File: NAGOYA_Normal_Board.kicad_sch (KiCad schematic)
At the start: 99 parts, among them CN1 XT30-M, CN13 value, CN14 RefereeSystem, CN15 micro_B, CN2 XT30-M, CN3 XT30-F, CN4 XT30-F, CN5 XT30-F, CN6 XT30-F, J1 debug, J10 CAN3, J13 CAN3, J14 CAN3, J5 CAN3, J6 CAN3, J7 CAN3, J8 CAN3, J9 CAN3, Q2 DDTC114EUA-7-F, Q4 DDTC114EUA-7-F, Q5 DDTC114EUA-7-F, Q6 DDTC114EUA-7-F, U1 Teensy4.1, U2 TCAN1042HVDR, U3 TCAN1042HVDR, U4 TCAN1042HVDR, U5 FT234XD, U6 TLP172AM, U7 BNO055, U8 ADuM121N, U9 LXES11DAA2-137, Y2 32.768 k

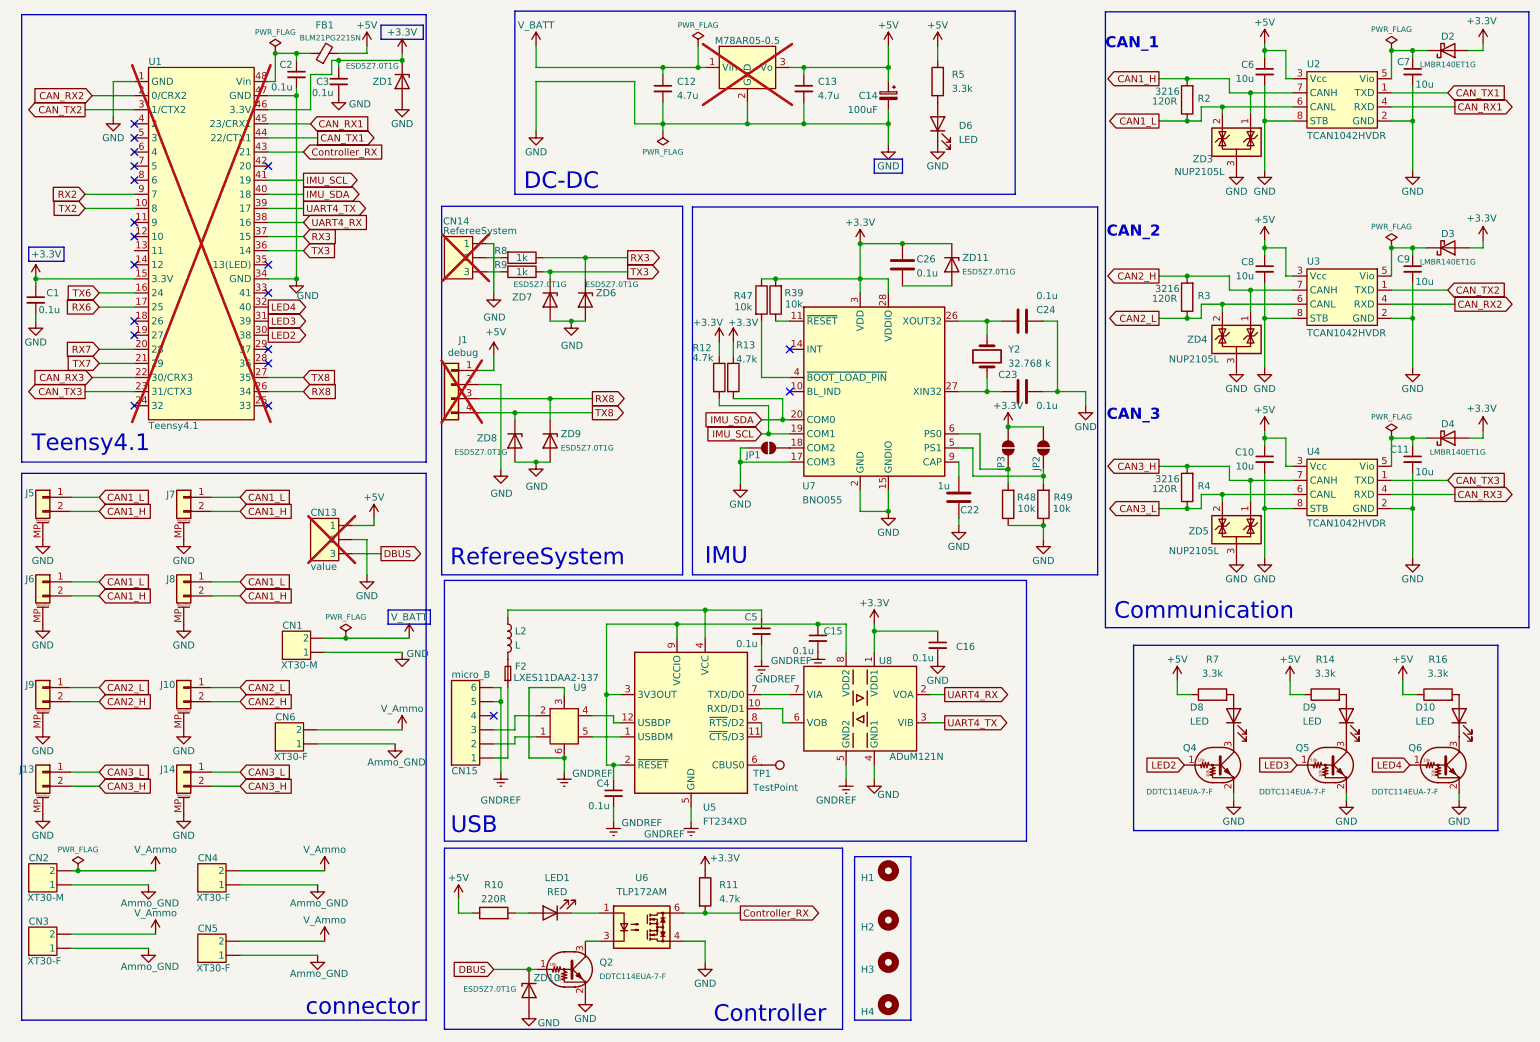
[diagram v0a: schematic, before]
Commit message: USBシリアルを絶縁
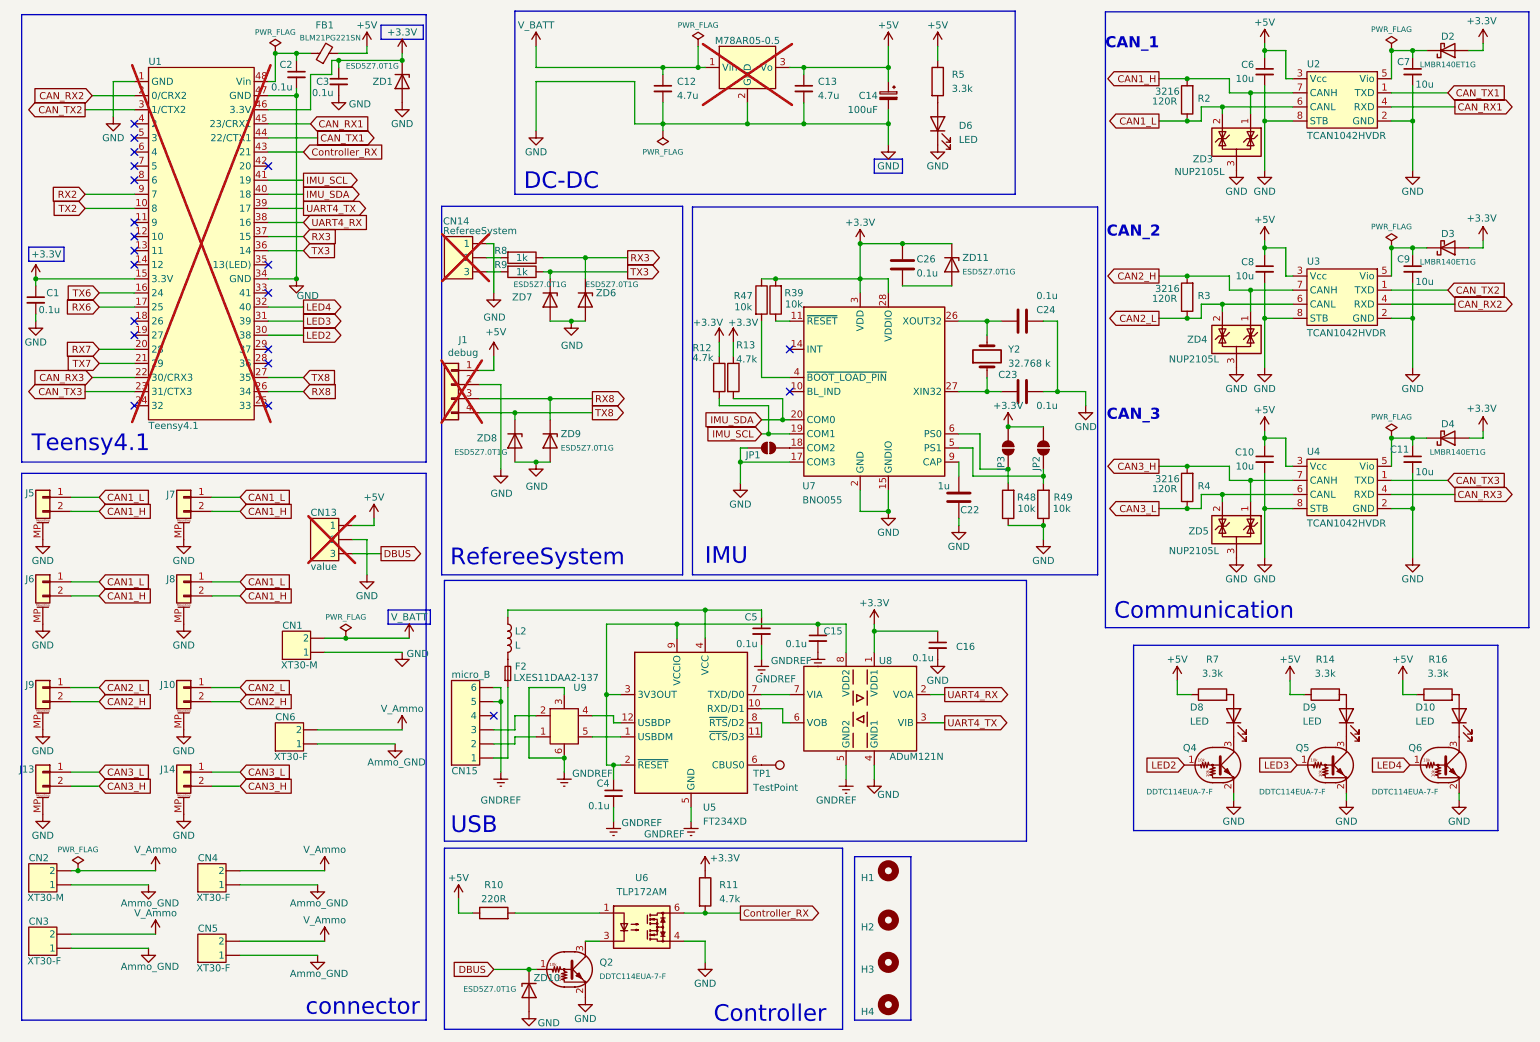
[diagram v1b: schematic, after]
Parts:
- removed LED1: RED, LED_SMD:LED_0603_1608Metric, symbol Device:LED
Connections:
- net at U6.1: now also R10.2
- no-connect marks 20 -> 21
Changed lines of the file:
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@@
 	)
 	(no_connect
+		(at 33.02 55.88)
+	)
+	(no_connect
 		(at 57.15 63.5)
 	)
@@
 	(wire
 		(pts
+			(xy 57.15 68.58) (xy 63.5 68.58)
+		)
+		(stroke
+			(width 0)
+			(type default)
+		)
+	)
+	(wire
+		(pts
 			(xy 236.728 55.372) (xy 236.728 56.642)
 		)
@@
 	(wire
 		(pts
+			(xy 57.15 71.12) (xy 63.5 71.12)
+		)
+		(stroke
+			(width 0)
+			(type default)
+		)
+	)
+	(wire
+		(pts
 			(xy 105.41 25.4) (xy 105.41 34.29)
 		)
@@
 	(wire
 		(pts
+			(xy 57.15 66.04) (xy 63.5 66.04)
+		)
+		(stroke
+			(width 0)
+			(type default)
+		)
+	)
+	(wire
+		(pts
 			(xy 107.95 82.55) (xy 107.95 86.36)
 		)
@@
 	(wire
 		(pts
-			(xy 104.14 175.26) (xy 101.6 175.26)
+			(xy 101.6 175.26) (xy 116.84 175.26)
 		)
 		(stroke
@@
 	(wire
 		(pts
-			(xy 111.76 175.26) (xy 116.84 175.26)
-		)
-		(stroke
-			(width 0)
-			(type default)
-		)
-	)
-	(wire
-		(pts
 			(xy 104.14 134.62) (xy 104.14 147.32)
 		)
@@
 	(global_label "LED4"
 		(shape output)
-		(at 57.15 66.04 0)
+		(at 63.5 66.04 0)
 		(fields_autoplaced yes)
 		(effects
@@
 		)
 		(property "Intersheetrefs" "${INTERSHEET_REFS}"
-			(at 64.7918 66.04 0)
+			(at 71.1418 66.04 0)
 			(effects
 				(font
@@
 	(global_label "LED3"
 		(shape output)
-		(at 57.15 68.58 0)
+		(at 63.5 68.58 0)
 		(fields_autoplaced yes)
 		(effects
@@
 		)
 		(property "Intersheetrefs" "${INTERSHEET_REFS}"
-			(at 64.7918 68.58 0)
+			(at 71.1418 68.58 0)
 			(effects
 				(font
@@
 	(global_label "LED2"
 		(shape output)
-		(at 57.15 71.12 0)
+		(at 63.5 71.12 0)
 		(fields_autoplaced yes)
 		(effects
@@
 		)
 		(property "Intersheetrefs" "${INTERSHEET_REFS}"
-			(at 64.7918 71.12 0)
+			(at 71.1418 71.12 0)
 			(effects
 				(font
@@
 	)
 	(symbol
-		(lib_id "Device:LED")
-		(at 107.95 175.26 180)
-		(unit 1)
-		(exclude_from_sim no)
-		(in_bom yes)
-		(on_board yes)
-		(dnp no)
-		(property "Reference" "LED1"
-			(at 109.22 168.91 0)
-			(effects
-				(font
-					(size 1.27 1.27)
-				)
-			)
-		)
-		(property "Value" "RED"
-			(at 109.22 171.45 0)
-			(effects
-				(font
-					(size 1.27 1.27)
-				)
-			)
-		)
-		(property "Footprint" "LED_SMD:LED_0603_1608Metric"
-			(at 107.95 175.26 0)
-			(effects
-				(font
-					(size 1.27 1.27)
-				)
-				(hide yes)
-			)
-		)
-		(property "Datasheet" "https://wmsc.lcsc.com/wmsc/upload/file/pdf/v2/lcsc/2304140030_ROHM-Semicon-SML-D12U8WT86_C510027.pdf"
-			(at 107.95 175.26 0)
-			(effects
-				(font
-					(size 1.27 1.27)
-				)
-				(hide yes)
-			)
-		)
-		(property "Description" "Light emitting diode"
-			(at 107.95 175.26 0)
-			(effects
-				(font
-					(size 1.27 1.27)
-				)
-				(hide yes)
-			)
-		)
-		(property "メーカ" ""
-			(at 107.95 175.26 90)
-			(effects
-				(font
-					(size 1.27 1.27)
-				)
-				(hide yes)
-			)
-		)
-		(property "購入先" "JLCPCB"
-			(at 107.95 175.26 90)
-			(effects
-				(font
-					(size 1.27 1.27)
-				)
-				(hide yes)
-			)
-		)
-		(property "型番" "SML-D12U8WT86"
-			(at 107.95 175.26 90)
-			(effects
-				(font
-					(size 1.27 1.27)
-				)
-				(hide yes)
-			)
-		)
-		(property "LCSC" "C510027"
-			(at 107.95 175.26 90)
-			(effects
-				(font
-					(size 1.27 1.27)
-				)
-				(hide yes)
-			)
-		)
-		(property "メーカー名" "Rohm"
-			(at 107.95 175.26 0)
-			(effects
-				(font
-					(size 1.27 1.27)
-				)
-				(hide yes)
-			)
-		)
-		(pin "2"
-		)
-		(pin "1"
-		)
-		(instances
-			(project "NAGOYA_Normal_Board"
-				(path "/21c37265-f169-4bc1-832f-6fa8bb337745"
-					(reference "LED1")
-					(unit 1)
-				)
-			)
-		)
-	)
-	(symbol
 		(lib_id "Device:R")
 		(at 97.79 175.26 90)
@@
 		)
 		(property "Value" "0.1u"
-			(at 151.638 128.016 0)
+			(at 150.368 126.746 0)
 			(effects
 				(font

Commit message: 発注用データ
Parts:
- added R50, R51, R52, R53: 10k, Resistor_SMD:R_0603_1608Metric, symbol Device:R
- added SW1: SW_DIP_x04, Button_Switch_SMD:SW_DIP_SPSTx04_Slide_Copal_CHS-04A_W5.08mm_P1.27mm_JPin, symbol Switch:SW_DIP_x04
- C15, C16, C4, C5, CN1, CN2, CN3, CN4, CN5, CN6, F2, JP1, JP2, JP3, L2, TP1, U5, U9: now not fitted
- C22: LCSC (none) -> C15849
- C23, C24, C26: LCSC (none) -> C14663
- CN15: LCSC (none) -> C132563; now not fitted
- J10, J13, J14, J5, J6, J7, J8, J9: LCSC (none) -> C189893
- R39, R47, R48, R49: LCSC (none) -> C25804
- R8, R9: LCSC (none) -> C21190
- U6: LCSC (none) -> C2152276
- U7: LCSC (none) -> C93216
- U8: LCSC (none) -> C660274; now not fitted
- Y2: LCSC (none) -> C32346
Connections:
- net +3.3V: now also R50.2, R51.2, R52.2, R53.2
- net GND: now also SW1.5, SW1.6, SW1.7, SW1.8
- net DIP_SW_4: now reaches U1.11 (9)
- net DIP_SW_4: now also R53.1, SW1.4
- net DIP_SW_3: now reaches U1.12 (10)
- net DIP_SW_3: now also R52.1, SW1.3
- net DIP_SW_2: now reaches U1.13 (11)
- net DIP_SW_2: now also R51.1, SW1.2
- net DIP_SW_1: now reaches U1.14 (12)
- net DIP_SW_1: now also R50.1, SW1.1
- no-connect marks 21 -> 17
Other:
- moved on the sheet: C12, C13, C14, D6, M78AR05-0.5, R5

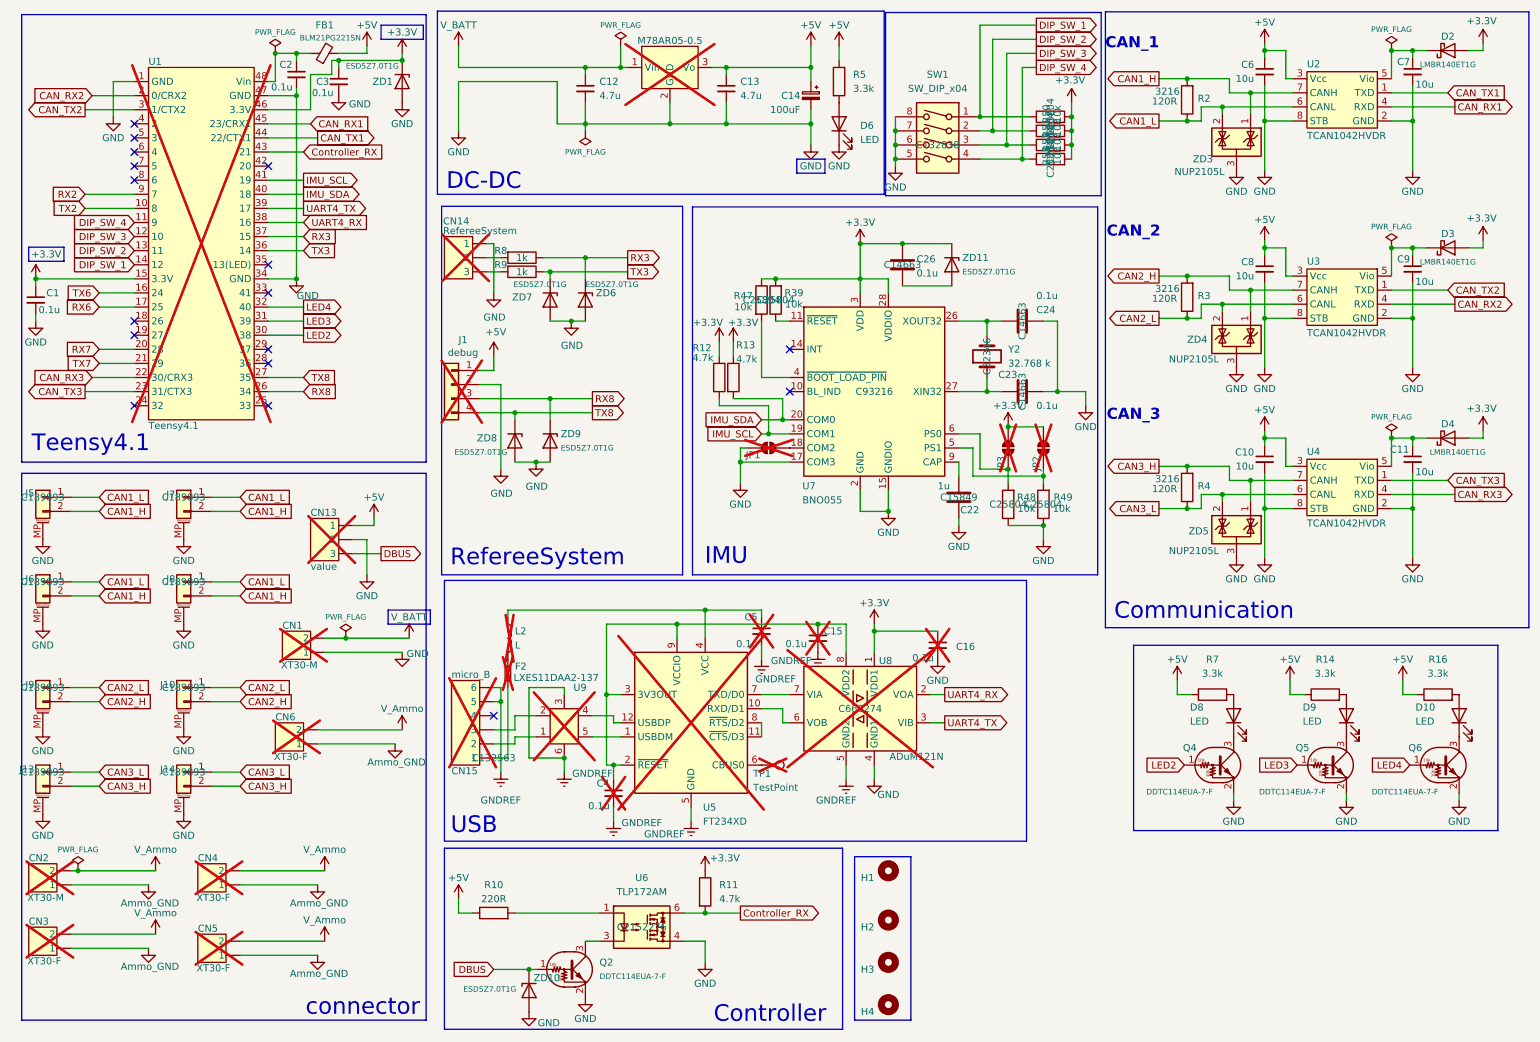
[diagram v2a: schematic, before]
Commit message: 発注用parameterを変更
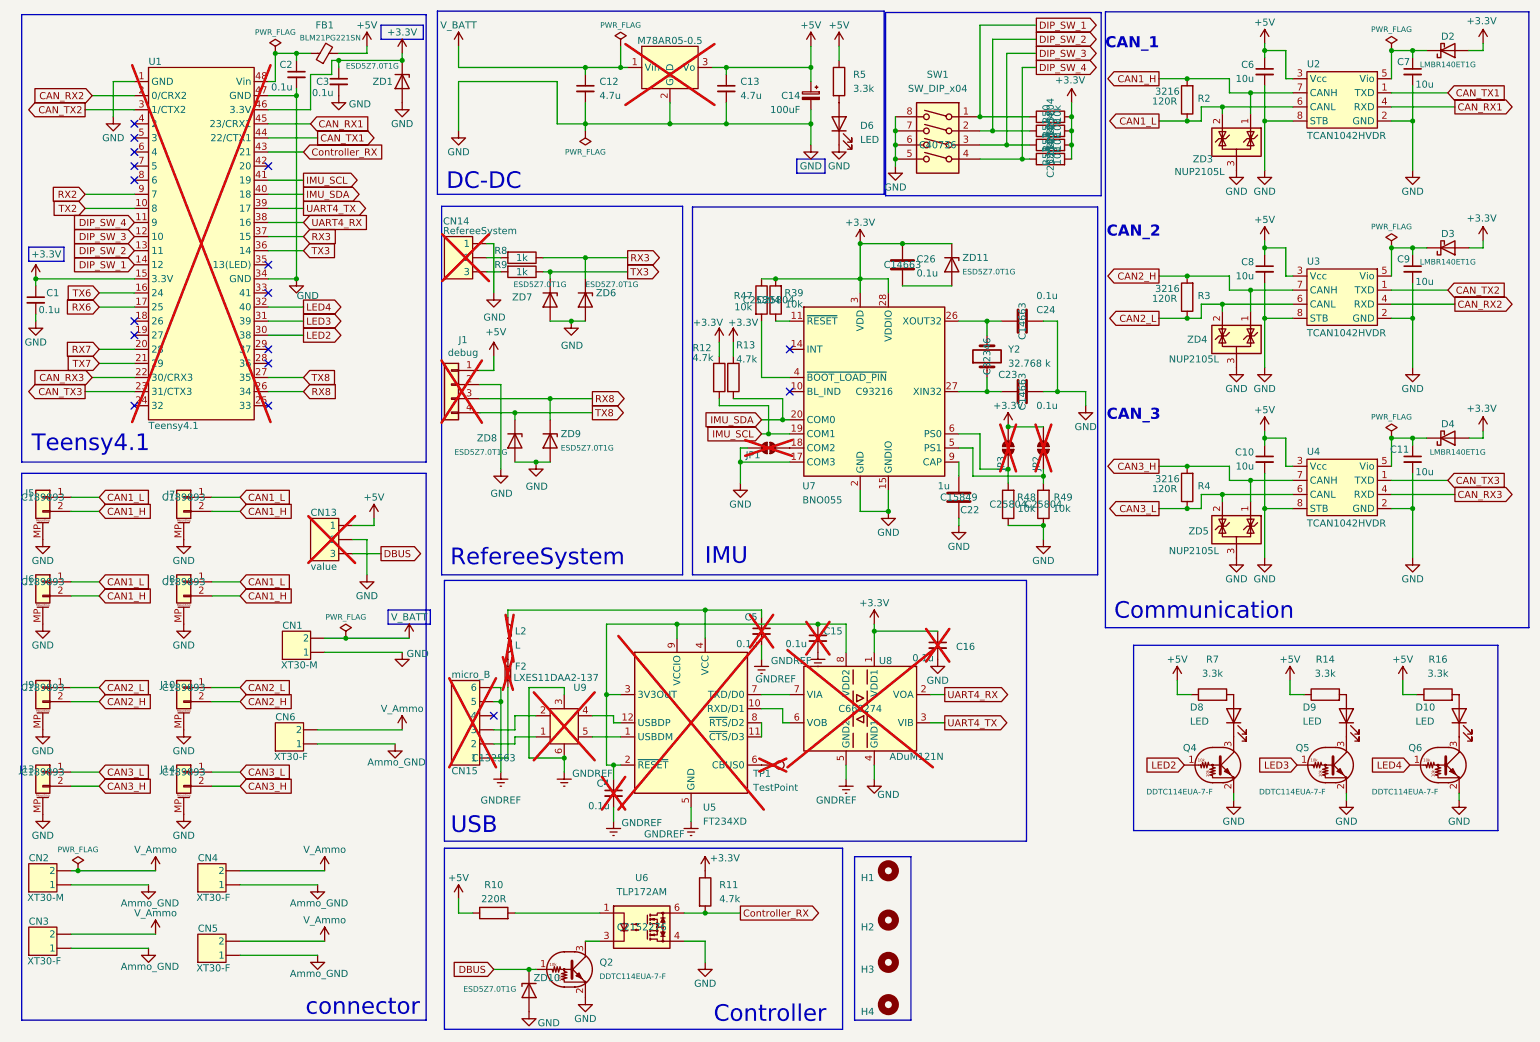
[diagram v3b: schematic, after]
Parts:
- CN1, CN2: now fitted
- CN3, CN4, CN5, CN6: LCSC C428721 -> C108769; now fitted
- JP1, JP2, JP3: now left out of the parts list
- SW1: footprint Button_Switch_SMD:SW_DIP_SPSTx04_Slide_Copal_CHS-04A_W5.08mm_P1.27mm_JPin -> Button_Switch_SMD:SW_DIP_SPSTx04_Slide_Copal_CHS-04B_W7.62mm_P1.27mm; LCSC C132838 -> C40736
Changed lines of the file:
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@@
 		(in_bom yes)
 		(on_board yes)
-		(dnp yes)
+		(dnp no)
 		(property "Reference" "CN6"
 			(at 58.42 139.192 0)
@@
 			)
 		)
-		(property "LCSC" "C428721"
+		(property "LCSC" "C108769"
 			(at 66.04 144.78 0)
 			(effects
@@
 		(in_bom yes)
 		(on_board yes)
-		(dnp yes)
+		(dnp no)
 		(property "Reference" "CN2"
 			(at 13.97 164.592 0)
@@
 		(in_bom yes)
 		(on_board yes)
-		(dnp yes)
+		(dnp no)
 		(property "Reference" "CN1"
 			(at 59.69 122.682 0)
@@
 		(at 147.32 91.44 180)
 		(unit 1)
-		(exclude_from_sim no)
-		(in_bom yes)
+		(exclude_from_sim yes)
+		(in_bom no)
 		(on_board yes)
 		(dnp yes)
@@
 		(in_bom yes)
 		(on_board yes)
-		(dnp yes)
+		(dnp no)
 		(property "Reference" "CN3"
 			(at 13.97 176.022 0)
@@
 			)
 		)
-		(property "LCSC" "C428721"
+		(property "LCSC" "C108769"
 			(at 21.59 181.61 0)
 			(effects
@@
 			)
 		)
-		(property "Footprint" "Button_Switch_SMD:SW_DIP_SPSTx04_Slide_Copal_CHS-04A_W5.08mm_P1.27mm_JPin"
+		(property "Footprint" "Button_Switch_SMD:SW_DIP_SPSTx04_Slide_Copal_CHS-04B_W7.62mm_P1.27mm"
 			(at 177.8 36.83 0)
 			(effects
@@
 			)
 		)
-		(property "LCSC" "C132838"
+		(property "LCSC" "C40736 "
 			(at 177.8 36.83 0)
 			(effects
@@
 		(at 190.5 91.44 270)
 		(unit 1)
-		(exclude_from_sim no)
-		(in_bom yes)
+		(exclude_from_sim yes)
+		(in_bom no)
 		(on_board yes)
 		(dnp yes)
@@
 		(at 196.85 91.44 270)
 		(unit 1)
-		(exclude_from_sim no)
-		(in_bom yes)
+		(exclude_from_sim yes)
+		(in_bom no)
 		(on_board yes)
 		(dnp yes)
@@
 		(in_bom yes)
 		(on_board yes)
-		(dnp yes)
+		(dnp no)
 		(property "Reference" "CN4"
 			(at 44.45 164.592 0)
@@
 			)
 		)
-		(property "LCSC" "C428721"
+		(property "LCSC" "C108769"
 			(at 52.07 170.18 0)
 			(effects
@@
 		(in_bom yes)
 		(on_board yes)
-		(dnp yes)
+		(dnp no)
 		(property "Reference" "CN5"
 			(at 44.45 177.292 0)
@@
 			)
 		)
-		(property "LCSC" "C428721"
+		(property "LCSC" "C108769"
 			(at 52.07 182.88 0)
 			(effects
